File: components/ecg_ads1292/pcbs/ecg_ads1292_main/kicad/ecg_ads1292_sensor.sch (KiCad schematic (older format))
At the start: 34 parts, among them IC1 ADS1292, U1 TPS73033DBVT

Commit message: schematic passes erc with two accpted warnings
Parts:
- added R4: 100, Resistor_SMD:R_0603_1608Metric_Pad1.05x0.95mm_HandSolder, symbol component:R
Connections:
- net at C4.1, C5.1, L1.1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: now also R4.2; no longer U1.3 (EN)
- new net: R4.1, U1.3 (EN)
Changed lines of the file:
@@
 Title "lifesensor ecg ads1292 sensor"
 Date "2020-04-27"
-Rev "0.1"
+Rev "0"
 Comp "Cadus e.V."
 Comment1 "n.p.: do not place"
@@
 	1600 6850 1600 6550
 Wire Wire Line
-	2250 6750 2450 6750
-Wire Wire Line
-	2250 6550 2250 6750
+	2050 6750 2100 6750
+Wire Wire Line
+	2050 6550 2050 6750
 Wire Wire Line
 	7200 3900 7300 3900
@@
 Connection ~ 1900 6550
 Connection ~ 1600 6550
-Connection ~ 2250 6550
+Connection ~ 2050 6550
 Connection ~ 7800 850
 NoConn ~ 7200 4000
@@
 	7850 4250 7850 4300
 Wire Wire Line
-	1900 6550 2250 6550
+	1900 6550 2050 6550
 Wire Wire Line
 	1600 6550 1900 6550
 Wire Wire Line
-	2250 6550 2450 6550
+	2050 6550 2450 6550
 $Comp
 L component:ADS1292 IC?
@@
 Wire Wire Line
 	4100 850  5850 850
+$Comp
+L component:R R4
+U 1 1 5EA9A4D2
+P 2250 6750
+F 0 "R4" V 2150 6650 50  0000 L CNN
+F 1 "100" V 2250 6750 50  0000 C CNN
+F 2 "Resistor_SMD:R_0603_1608Metric_Pad1.05x0.95mm_HandSolder" V 2180 6750 50  0001 C CNN
+F 3 "" H 2250 6750 50  0001 C CNN
+F 4 "1739145" H -5200 3750 50  0001 C CNN "Best.Nr."
+F 5 "Farnell" H -5200 3750 50  0001 C CNN "Distributor"
+F 6 "1739145" H -5200 3750 50  0001 C CNN "Farnell"
+	1    2250 6750
+	0    1    1    0
+$EndComp
+Wire Wire Line
+	2400 6750 2450 6750
 $EndSCHEMATC

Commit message: ecg_ads1292: fix symbol library paths
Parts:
- C1, C2, C3: value 3n -> 3n C0G 50V 5%; symbol component:C_Small -> ecg_ads1292_main:C_Small
- C10, C11, C13, C14, C15, C16, C17, C18, C19, C20, C21, C6, C7: symbol component:C_Small -> ecg_ads1292_main:C_Small
- C4, C5, C8, C9: symbol component:C -> ecg_ads1292_main:C
- IC1: symbol component:ADS1292 -> ecg_ads1292_main:ADS1292
- L1: symbol component:Ferrite_Bead_Small -> ecg_ads1292_main:Ferrite_Bead_Small
- R10, R11, R12, R13, R14, R15, R16, R17, R18, R19, R4, R9: symbol component:R -> ecg_ads1292_main:R
- U1: symbol component:TPS73033DBVT -> ecg_ads1292_main:TPS73033DBVT
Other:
- moved on the sheet: C1, C2, C3, R10, R11, R9

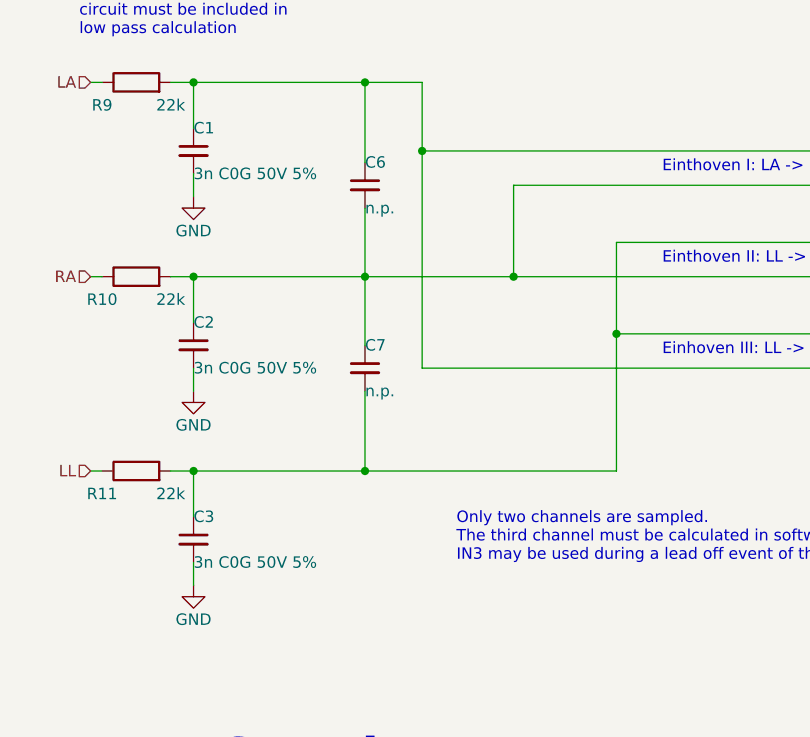
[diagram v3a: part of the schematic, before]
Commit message: ecg_ads1292 improve input filter circuit
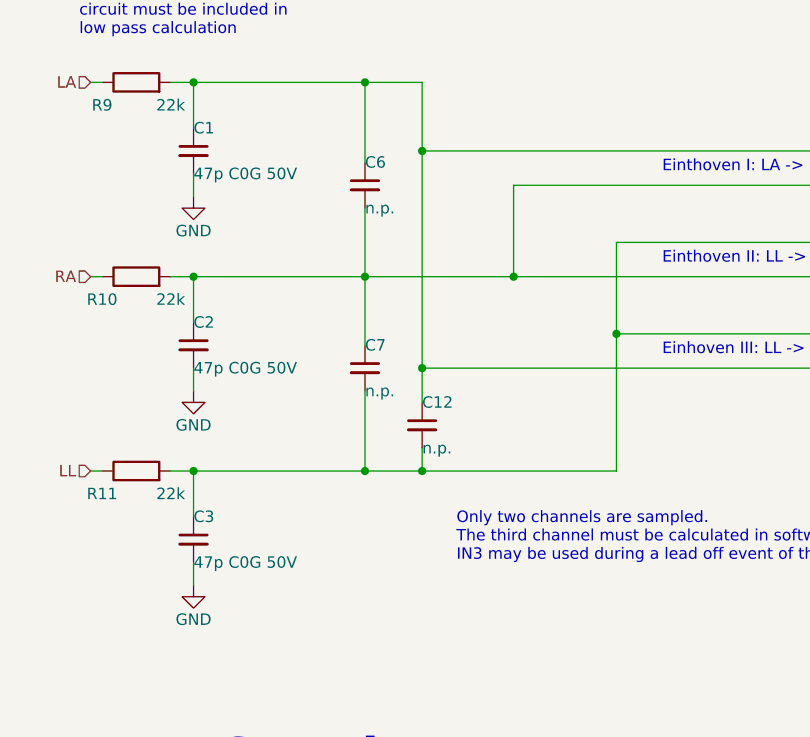
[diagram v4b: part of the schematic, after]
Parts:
- added C12: n.p., Capacitor_SMD:C_0603_1608Metric_Pad1.05x0.95mm_HandSolder, symbol ecg_ads1292_main:C_Small
- C1, C2, C3: value 3n C0G 50V 5% -> 47p C0G 50V
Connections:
- net ads_in1_p: now also C12.1
- net ads_in2_p: now also C12.2
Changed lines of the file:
@@
 P 1200 5250
 F 0 "C3" H 1200 5350 50  0000 L CNN
-F 1 "3n C0G 50V 5%" H 1200 5150 50  0000 L CNN
+F 1 "47p C0G 50V" H 1200 5150 50  0000 L CNN
 F 2 "Capacitor_SMD:C_0603_1608Metric_Pad1.05x0.95mm_HandSolder" H 1200 5250 50  0001 C CNN
 F 3 "" H 1200 5250 50  0001 C CNN
@@
 P 1200 4400
 F 0 "C2" H 1200 4500 50  0000 L CNN
-F 1 "3n C0G 50V 5%" H 1200 4300 50  0000 L CNN
+F 1 "47p C0G 50V" H 1200 4300 50  0000 L CNN
 F 2 "Capacitor_SMD:C_0603_1608Metric_Pad1.05x0.95mm_HandSolder" H 1200 4400 50  0001 C CNN
 F 3 "" H 1200 4400 50  0001 C CNN
@@
 P 1200 3550
 F 0 "C1" H 1200 3650 50  0000 L CNN
-F 1 "3n C0G 50V 5%" H 1200 3450 50  0000 L CNN
+F 1 "47p C0G 50V" H 1200 3450 50  0000 L CNN
 F 2 "Capacitor_SMD:C_0603_1608Metric_Pad1.05x0.95mm_HandSolder" H 1200 3550 50  0001 C CNN
 F 3 "" H 1200 3550 50  0001 C CNN
@@
 	2400 6750 2450 6750
 Wire Wire Line
-	1950 4950 3050 4950
+	1950 4950 2200 4950
+$Comp
+L ecg_ads1292_main:C_Small C12
+U 1 1 5EB50558
+P 2200 4750
+F 0 "C12" H 2200 4850 50  0000 L CNN
+F 1 "n.p." H 2200 4650 50  0000 L CNN
+F 2 "Capacitor_SMD:C_0603_1608Metric_Pad1.05x0.95mm_HandSolder" H 2200 4750 50  0001 C CNN
+F 3 "" H 2200 4750 50  0001 C CNN
+F 4 "1865491" H -50 250 50  0001 C CNN "Best.Nr."
+F 5 "C0G/NPO" H -50 250 50  0001 C CNN "Comment"
+F 6 "Farnell" H -50 250 50  0001 C CNN "Distributor"
+F 7 "1865491" H -50 250 50  0001 C CNN "Farnell"
+	1    2200 4750
+	1    0    0    -1
+$EndComp
+Wire Wire Line
+	2200 4650 2200 4500
+Connection ~ 2200 4500
+Wire Wire Line
+	2200 4850 2200 4950
+Connection ~ 2200 4950
+Wire Wire Line
+	2200 4950 3050 4950
 $EndSCHEMATC

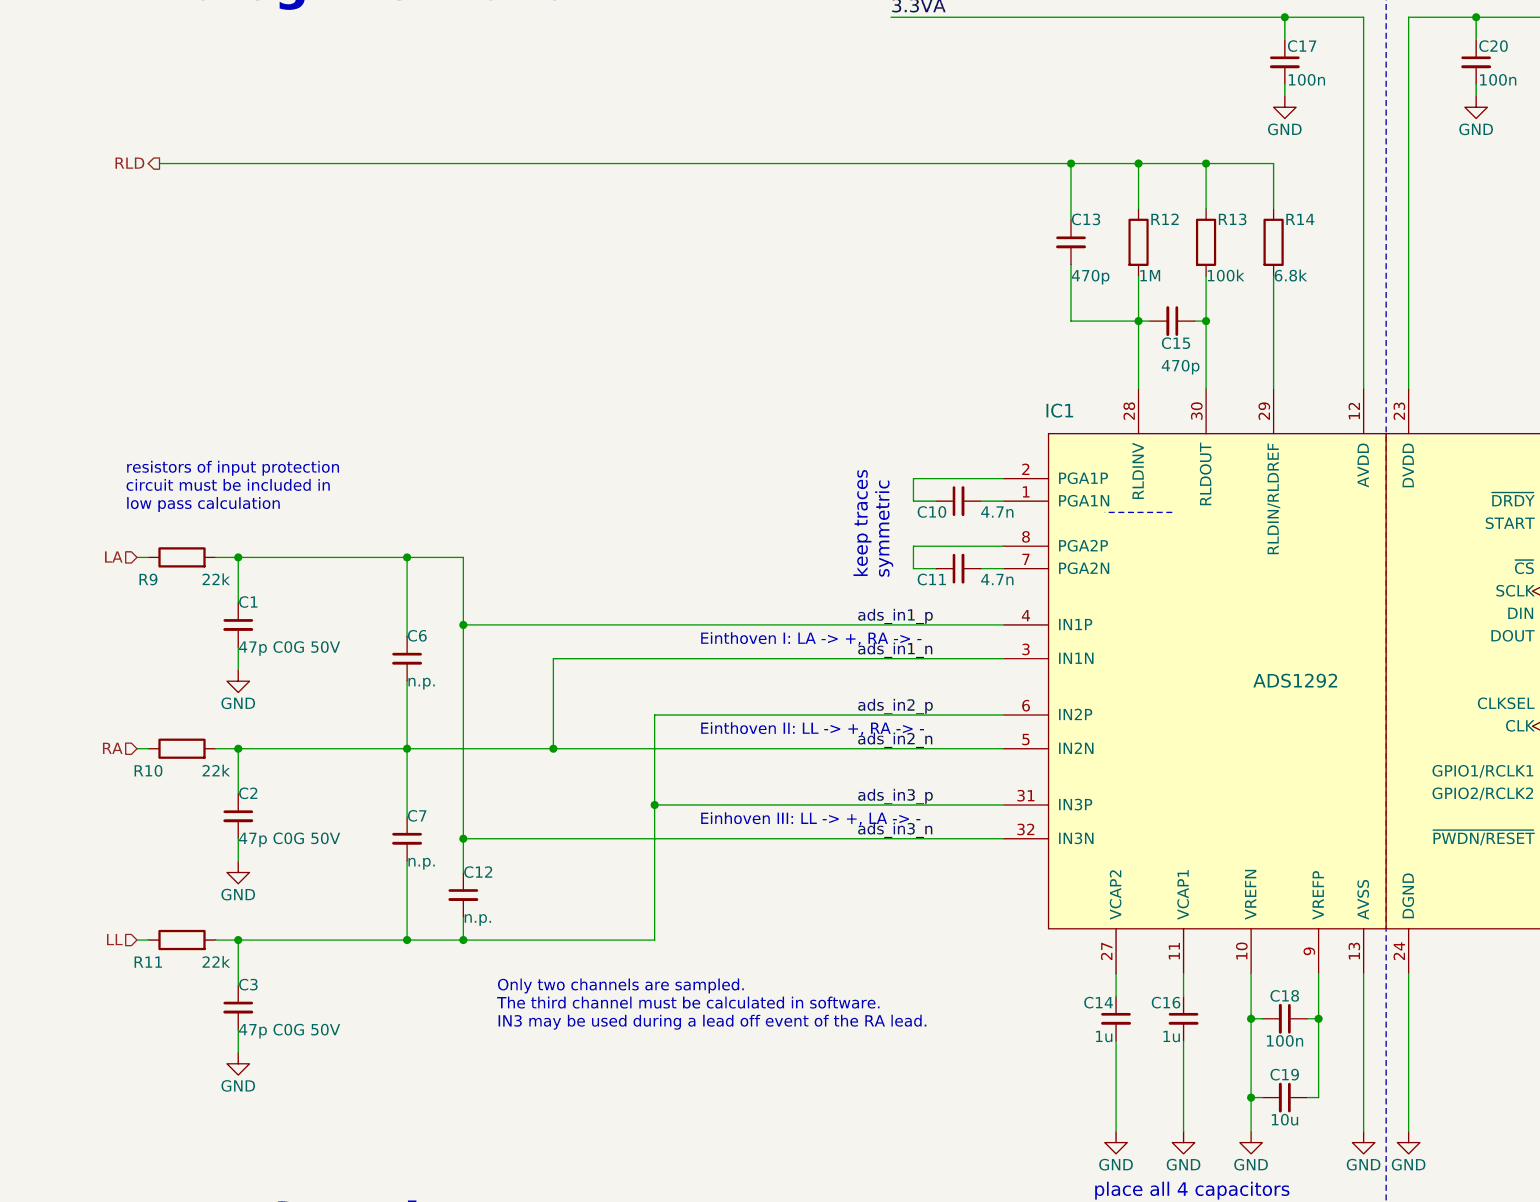
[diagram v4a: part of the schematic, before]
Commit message: ecg_ads1292: update part fields
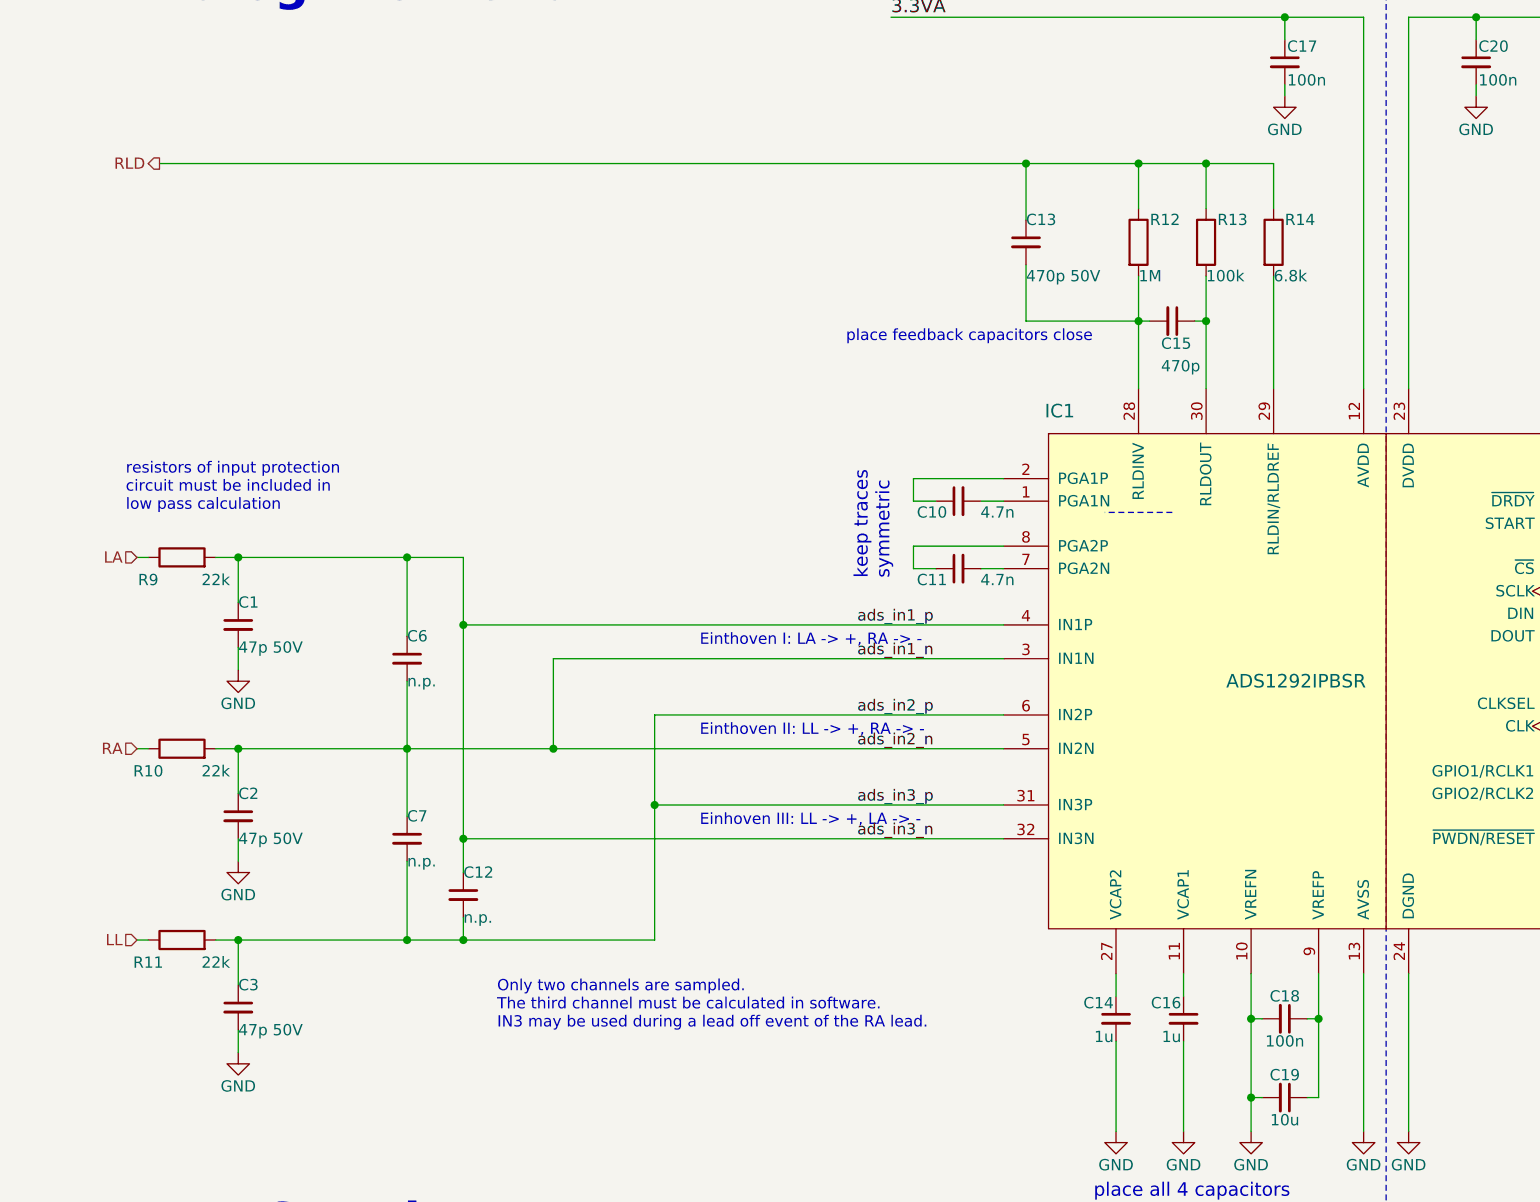
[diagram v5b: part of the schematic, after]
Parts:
- C1, C2, C3: value 47p C0G 50V -> 47p 50V; Best.Nr. 1865491 -> (none); Comment C0G/NPO -> (none); Distributor Farnell -> (none); Farnell 1865491 -> (none); PN Farnell (none) -> 1865491
- C10, C11: Best.Nr. 2611918 -> (none); Comment C0G/NPO -> (none); Distributor Farnell -> (none); Farnell 2611918 -> (none); PN Farnell (none) -> 2611918
- C12, C6, C7: Best.Nr. 1865491 -> (none); Comment C0G/NPO -> (none); Distributor Farnell -> (none); Farnell 1865491 -> (none); PN Farnell (none) -> 1865491
- C13: value 470p -> 470p 50V; Comment C0G/NPO -> (none); PN Farnell (none) -> 2627442
- C14, C16, C21: Best.Nr. 2112849 -> (none); Comment X7R -> (none); Distributor Farnell -> (none); Farnell 2112849 -> (none); PN Farnell (none) -> 2112849
- C15: Comment C0G/NPO -> (none); PN Farnell (none) -> 2627442
- C17, C20: Best.Nr. 1907318 -> (none); Comment X7R -> (none); Distributor Farnell -> (none); Farnell 1907318 -> (none); PN Farnell (none) -> 1907318
- C18: Best.Nr. 2494294 -> (none); Comment C0G/NPO -> (none); Distributor Farnell -> (none); Farnell 2494294 -> (none); PN Farnell (none) -> 2494294
- C19: Best.Nr. 1889276 -> (none); Comment X7R -> (none); Distributor Farnell -> (none); Farnell 1889276 -> (none); PN Farnell (none) -> 1889276
- C4, C9: Best.Nr. 1797012 -> (none); Distributor Farnell -> (none); Farnell 1797012 -> (none); PN Farnell (none) -> 1797012
- C5: Best.Nr. 1907318 -> (none); Distributor Farnell -> (none); Farnell 1907318 -> (none); PN Farnell (none) -> 1907318
- C8: Best.Nr. 2496825 -> (none); Distributor Farnell -> (none); Farnell 2496825 -> (none); PN Farnell (none) -> 2496825
- IC1: value ADS1292 -> ADS1292IPBSR; Created Lukas Holzapfel -> (none); PN Farnell (none) -> 3116599
- L1: Best.Nr. 1669719 -> (none); Distributor Farnell -> (none); Farnell 1669719 -> (none); PN Farnell (none) -> 1669719
- R10, R11, R9: Best.Nr. 1469825 -> (none); Distributor Farnell -> (none); Farnell 1469825 -> (none); PN Farnell (none) -> 1469825
- R12: Best.Nr. 1469746 -> (none); Distributor Farnell -> (none); Farnell 1469746 -> (none); PN Farnell (none) -> 1469746
- R13: Best.Nr. 1692517 -> (none); Distributor Farnell -> (none); Farnell 1692517 -> (none); PN Farnell (none) -> 1692517
- R14, R18, R19: Best.Nr. 1738916 -> (none); Distributor Farnell -> (none); Farnell 1738916 -> (none); PN Farnell (none) -> 1738916
- R15, R16, R17, R4: Best.Nr. 1739145 -> (none); Distributor Farnell -> (none); Farnell 1739145 -> (none); PN Farnell (none) -> 1739145
- U1: Best.Nr. 1135395 -> (none); Distributor Farnell -> (none); Farnell 1135395 -> (none); PN Farnell (none) -> 1135395
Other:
- note added: "place feedback capacitors close"
- moved on the sheet: C13
